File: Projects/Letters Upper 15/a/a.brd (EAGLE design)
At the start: 16.5 x 21.6 mm, 42 parts

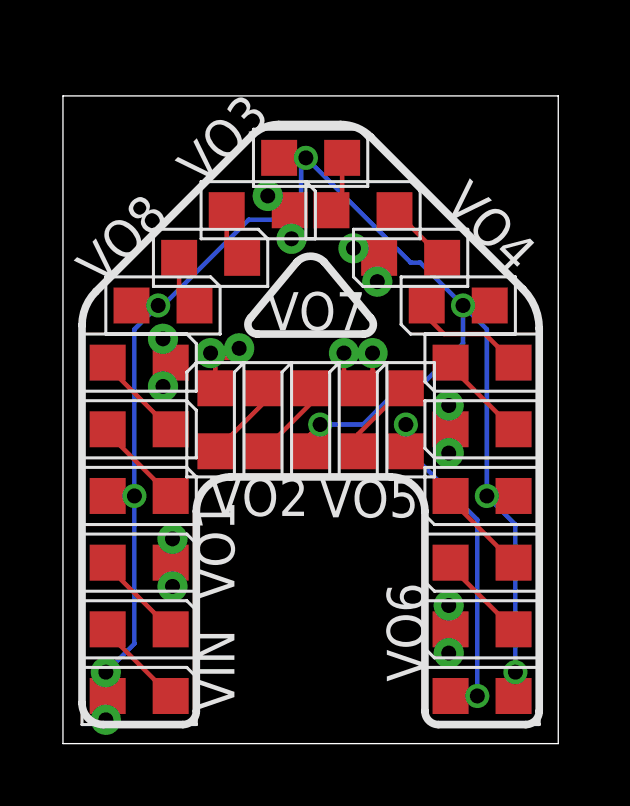
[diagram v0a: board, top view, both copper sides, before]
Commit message: 
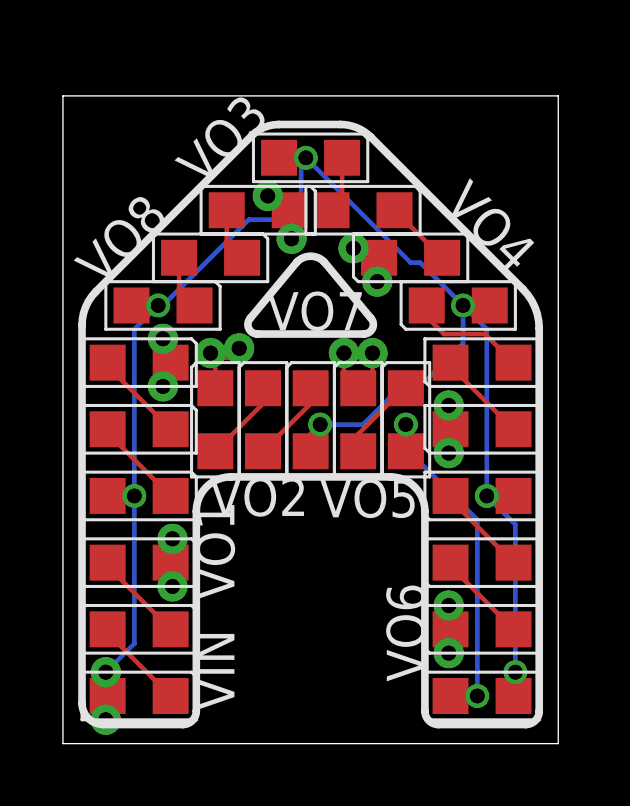
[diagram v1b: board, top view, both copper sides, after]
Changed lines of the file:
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@@
 <?xml version="1.0" encoding="utf-8"?>
 <!DOCTYPE eagle SYSTEM "eagle.dtd">
-<eagle version="7.1.0">
+<eagle version="7.2.0">
 <drawing>
 <settings>
